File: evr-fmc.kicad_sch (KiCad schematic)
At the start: 0 parts

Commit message: Final Draft - Ready for review
Updates:
- Changed area behind FMC connector to match the new Osprey FMC template
  - This includes a new 12V LED, more robust power input traces, arranged elements for readability.

Things to do:
Round diff traces before generating fabrication files
Change name of project to 'trigger output fmc'
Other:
- title: FMC Template -> Trigger Output FMC
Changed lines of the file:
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@@
 	(paper "USLetter")
 	(title_block
-		(title "FMC Template")
-		(date "2026-01-26")
+		(title "Trigger Output FMC")
+		(date "2026-05-07")
 		(rev "1.0")
 		(company "SPDX-FileCopyrightText: 2025 Osprey DCS")

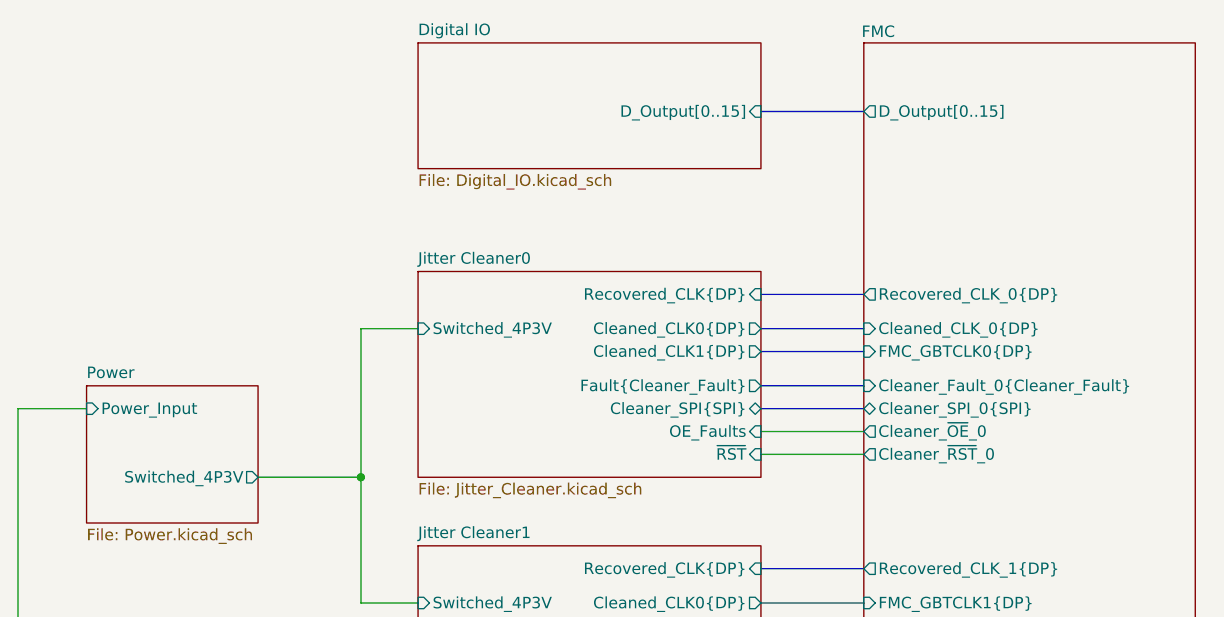
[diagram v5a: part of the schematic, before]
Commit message: Changed Trigger Outputs Topology
- Changed to a comp to digital TX design
- Added power section to support this change
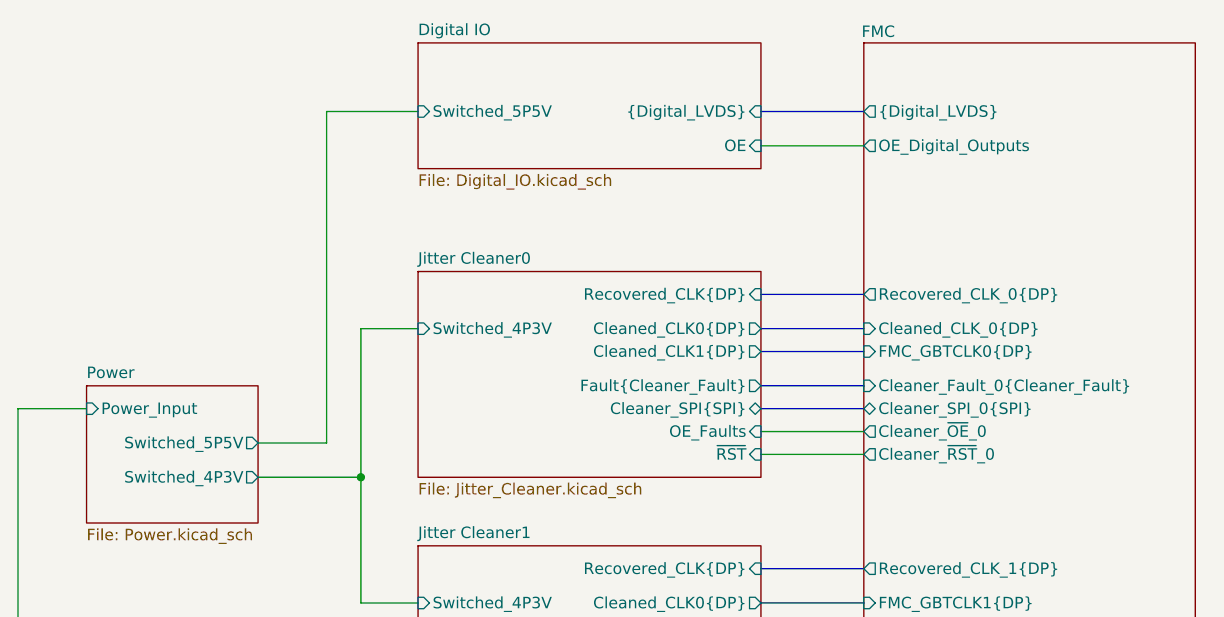
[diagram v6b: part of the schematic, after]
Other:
- sheet Digital IO ports: added OE, Switched_5P5V, {Digital_LVDS}; removed D_Output[0..15]
- sheet FMC ports: added OE_Digital_Outputs, {Digital_LVDS}; removed D_Output[0..15]
- sheet Power ports: added Switched_5P5V; removed none
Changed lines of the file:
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@@
+		)
+	)
+	(wire
+		(pts
+			(xy 161.29 50.8) (xy 172.72 50.8)
+		)
+		(stroke
+			(width 0)
+			(type default)
+		)
+	)
+	(wire
+		(pts
+			(xy 161.29 115.57) (xy 172.72 115.57)
+		)
+		(stroke
+			(width 0)
+			(type default)
+		)
+	)
+	(wire
+		(pts
+			(xy 105.41 83.82) (xy 113.03 83.82)
+		)
+		(stroke
+			(width 0)
+			(type default)
+		)
+	)
+	(bus
+		(pts
+			(xy 161.29 80.01) (xy 172.72 80.01)
+		)
+		(stroke
+			(width 0)
+			(type default)
+		)
+	)
+	(wire
+		(pts
+			(xy 113.03 46.99) (xy 123.19 46.99)
+		)
+		(stroke
+			(width 0)
+			(type default)
+		)
+	)
+	(bus
+		(pts
+			(xy 161.29 67.31) (xy 172.72 67.31)
+		)
+		(stroke
+			(width 0)
+			(type default)
+		)
+	)
+	(wire
+		(pts
+			(xy 113.03 83.82) (xy 113.03 46.99)
+		)
+		(stroke
+			(width 0)
+			(type default)
+		)
+	)
+	(wire
+		(pts
+			(xy 116.84 71.12) (xy 116.84 87.63)
+		)
+		(stroke
+			(width 0)
+			(type default)
+		)
+	)
+	(bus
+		(pts
+			(xy 161.29 97.79) (xy 172.72 97.79)
+		)
+		(stroke
+			(width 0)
+			(type default)
+		)
+	)
+	(wire
+		(pts
+			(xy 123.19 71.12) (xy 116.84 71.12)
+		)
+		(stroke
+			(width 0)
+			(type default)
+		)
+	)
+	(wire
+		(pts
+			(xy 78.74 80.01) (xy 86.36 80.01)
+		)
+		(stroke
+			(width 0)
+			(type default)
+		)
+	)
+	(wire
+		(pts
+			(xy 161.29 82.55) (xy 172.72 82.55)
+		)
+		(stroke
+			(width 0)
+			(type default)
+		)
+	)
+	(wire
+		(pts
+			(xy 116.84 101.6) (xy 123.19 101.6)
+		)
+		(stroke
+			(width 0)
+			(type default)
+		)
+	)
+	(bus
+		(pts
+			(xy 161.29 101.6) (xy 172.72 101.6)
+		)
+		(stroke
+			(width 0)
+			(type default)
+		)
+	)
+	(wire
+		(pts
+			(xy 161.29 140.97) (xy 172.72 140.97)
+		)
+		(stroke
+			(width 0)
+			(type default)
+		)
+	)
+	(wire
+		(pts
+			(xy 172.72 125.73) (xy 78.74 125.73)
+		)
+		(stroke
+			(width 0)
+			(type default)
+		)
+	)
+	(wire
+		(pts
+			(xy 78.74 125.73) (xy 78.74 80.01)
+		)
+		(stroke
+			(width 0)
+			(type default)
+		)
+	)
+	(wire
+		(pts
+			(xy 105.41 87.63) (xy 116.84 87.63)
+		)
+		(stroke
+			(width 0)
+			(type default)
+		)
+	)
+	(bus
+		(pts
+			(xy 161.29 77.47) (xy 172.72 77.47)
+		)
+		(stroke
+			(width 0)
+			(type default)
+		)
+	)
+	(wire
+		(pts
+			(xy 116.84 87.63) (xy 116.84 101.6)
+		)
+		(stroke
+			(width 0)
+			(type default)
+		)
+	)
+	(wire
+		(pts
+			(xy 161.29 113.03) (xy 172.72 113.03)
+		)
+		(stroke
+			(width 0)
+			(type default)
 		)
 	)
@@
 		(pts
 			(xy 161.29 46.99) (xy 172.72 46.99)
-		)
-		(stroke
-			(width 0)
-			(type default)
-		)
-	)
-	(wire
-		(pts
-			(xy 161.29 115.57) (xy 172.72 115.57)
-		)
-		(stroke
-			(width 0)
-			(type default)
-		)
-	)
-	(bus
-		(pts
-			(xy 161.29 80.01) (xy 172.72 80.01)
-		)
-		(stroke
-			(width 0)
-			(type default)
-		)
-	)
-	(bus
-		(pts
-			(xy 161.29 67.31) (xy 172.72 67.31)
-		)
-		(stroke
-			(width 0)
-			(type default)
-		)
-	)
-	(wire
-		(pts
-			(xy 116.84 71.12) (xy 116.84 87.63)
-		)
-		(stroke
-			(width 0)
-			(type default)
-		)
-	)
-	(bus
-		(pts
-			(xy 161.29 97.79) (xy 172.72 97.79)
-		)
-		(stroke
-			(width 0)
-			(type default)
-		)
-	)
-	(wire
-		(pts
-			(xy 123.19 71.12) (xy 116.84 71.12)
-		)
-		(stroke
-			(width 0)
-			(type default)
-		)
-	)
-	(wire
-		(pts
-			(xy 78.74 80.01) (xy 86.36 80.01)
-		)
-		(stroke
-			(width 0)
-			(type default)
-		)
-	)
-	(wire
-		(pts
-			(xy 161.29 82.55) (xy 172.72 82.55)
-		)
-		(stroke
-			(width 0)
-			(type default)
-		)
-	)
-	(wire
-		(pts
-			(xy 116.84 101.6) (xy 123.19 101.6)
-		)
-		(stroke
-			(width 0)
-			(type default)
-		)
-	)
-	(bus
-		(pts
-			(xy 161.29 101.6) (xy 172.72 101.6)
-		)
-		(stroke
-			(width 0)
-			(type default)
-		)
-	)
-	(wire
-		(pts
-			(xy 161.29 140.97) (xy 172.72 140.97)
-		)
-		(stroke
-			(width 0)
-			(type default)
-		)
-	)
-	(wire
-		(pts
-			(xy 172.72 125.73) (xy 78.74 125.73)
-		)
-		(stroke
-			(width 0)
-			(type default)
-		)
-	)
-	(wire
-		(pts
-			(xy 78.74 125.73) (xy 78.74 80.01)
-		)
-		(stroke
-			(width 0)
-			(type default)
-		)
-	)
-	(wire
-		(pts
-			(xy 105.41 87.63) (xy 116.84 87.63)
-		)
-		(stroke
-			(width 0)
-			(type default)
-		)
-	)
-	(bus
-		(pts
-			(xy 161.29 77.47) (xy 172.72 77.47)
-		)
-		(stroke
-			(width 0)
-			(type default)
-		)
-	)
-	(wire
-		(pts
-			(xy 116.84 87.63) (xy 116.84 101.6)
-		)
-		(stroke
-			(width 0)
-			(type default)
-		)
-	)
-	(wire
-		(pts
-			(xy 161.29 113.03) (xy 172.72 113.03)
 		)
 		(stroke
@@
 			)
 		)
-		(pin "D_Output[0..15]" output
-			(at 172.72 46.99 180)
-			(effects
-				(font
-					(size 1.27 1.27)
-				)
-				(justify left)
-			)
-		)
 		(pin "Cleaner_SPI_0{SPI}" bidirectional
 			(at 172.72 80.01 180)
@@
 		(pin "Cleaner_~{OE}_1" output
 			(at 172.72 113.03 180)
+			(effects
+				(font
+					(size 1.27 1.27)
+				)
+				(justify left)
+			)
+		)
+		(pin "{Digital_LVDS}" output
+			(at 172.72 46.99 180)
+			(effects
+				(font
+					(size 1.27 1.27)
+				)
+				(justify left)
+			)
+		)
+		(pin "OE_Digital_Outputs" output
+			(at 172.72 50.8 180)
 			(effects
 				(font
@@
 			)
 		)
+		(pin "Switched_5P5V" output
+			(at 105.41 83.82 0)
+			(effects
+				(font
+					(size 1.27 1.27)
+				)
+				(justify right)
+			)
+		)
 		(instances
 			(project "evr-fmc"
@@
 			)
 		)
-		(pin "D_Output[0..15]" input
+		(pin "{Digital_LVDS}" input
 			(at 161.29 46.99 0)
 			(effects
 				(font
+					(size 1.27 1.27)
+				)
+				(justify right)
+			)
+		)
+		(pin "Switched_5P5V" input
+			(at 123.19 46.99 180)
+			(effects
+				(font
+					(size 1.27 1.27)
+				)
+				(justify left)
+			)
+		)
+		(pin "OE" input
+			(at 161.29 50.8 0)
+			(effects
+				(font

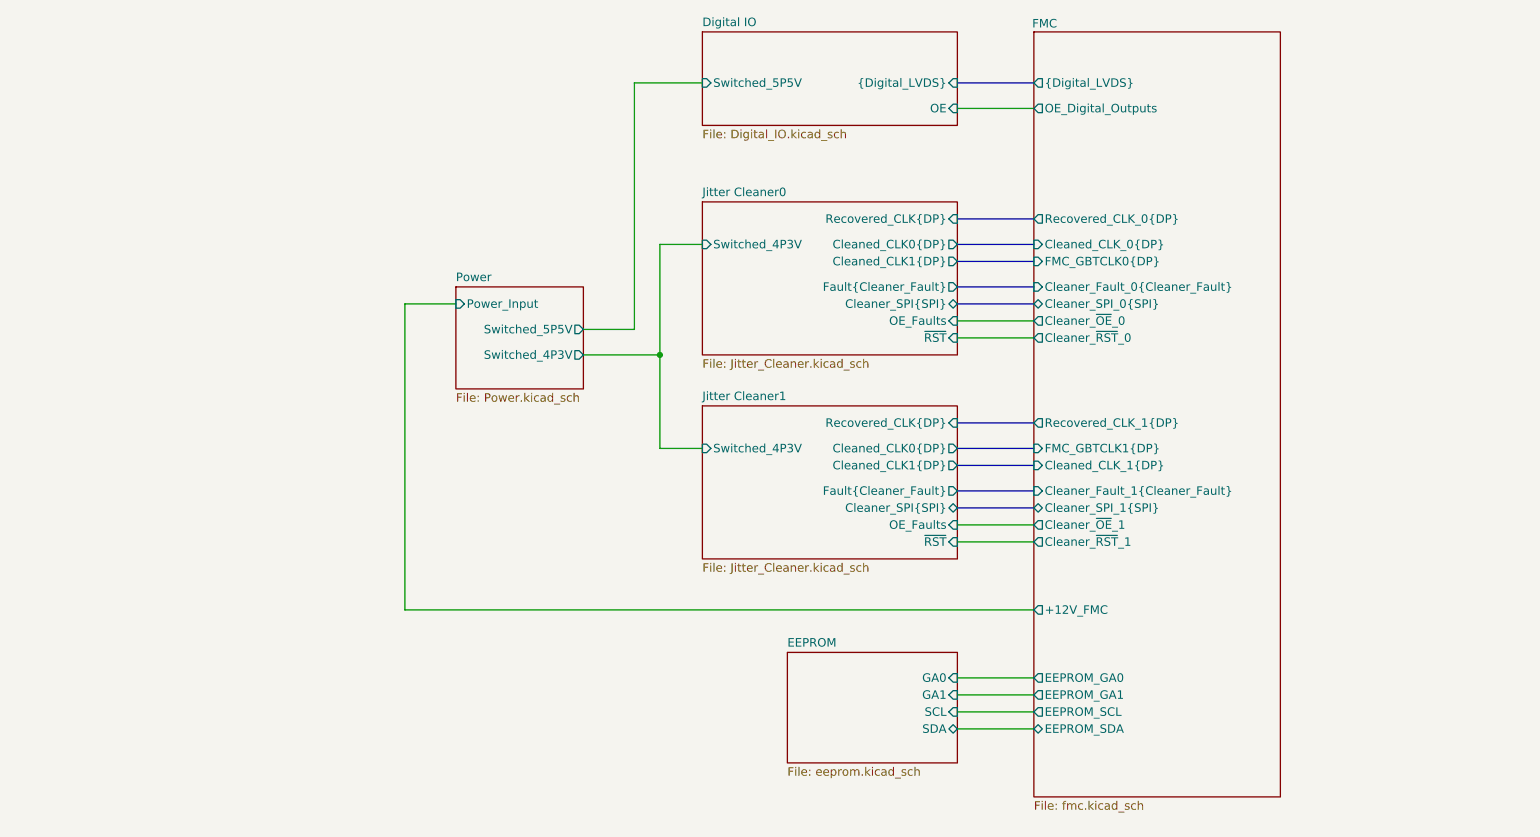
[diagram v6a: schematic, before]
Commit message: Added Level Shifter schematic & moved symbols
- Created a separate Level Shifter schematic to prepare use of some gates for Digital output enables.
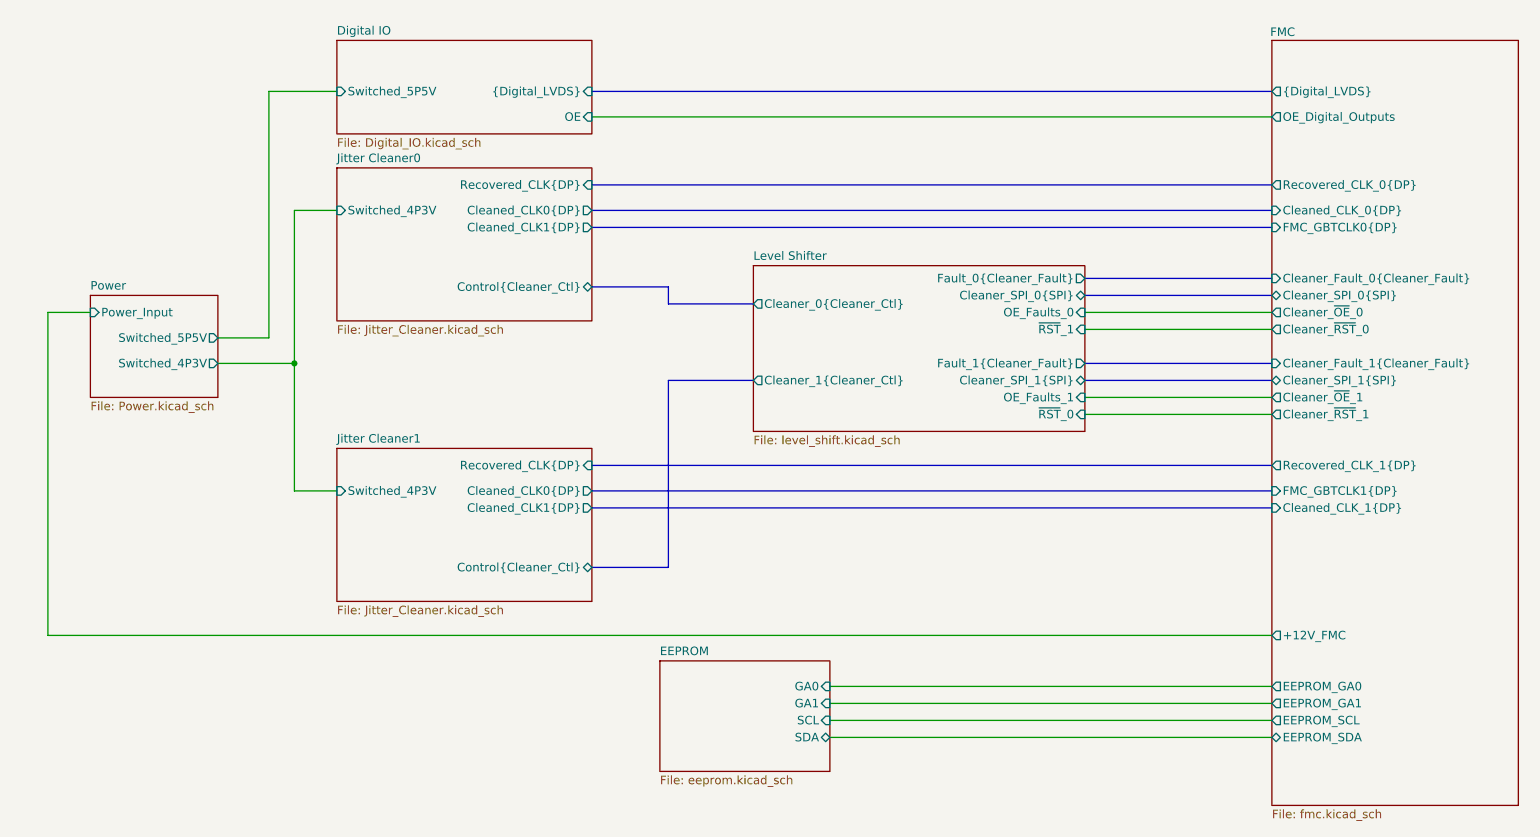
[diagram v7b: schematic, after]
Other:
- added sheet Level Shifter (level_shift.kicad_sch)
- sheet Jitter Cleaner0 ports: added Control{Cleaner_Ctl}; removed Cleaner_SPI{SPI}, Fault{Cleaner_Fault}, OE_Faults, ~{RST}
- sheet Jitter Cleaner1 ports: added Control{Cleaner_Ctl}; removed Cleaner_SPI{SPI}, Fault{Cleaner_Fault}, OE_Faults, ~{RST}
